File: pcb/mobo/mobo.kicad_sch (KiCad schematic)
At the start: 66 parts, among them J1 SWD_10, J2 PEEL_MOTOR, J3 DRIVE_MOTOR, J4 SW1, J5 SPRING_FINGERS, J6 SW2, J7 SW1, J8 USART1, J9 SWD_10, U1 STM32F031C6Tx, U2 STM32F031K6Ux, U4 AP1117-33, U5 MC34063AD, U6 MAX3078E, U7 DRV8837, U8 DRV8837, Y1 8MHz

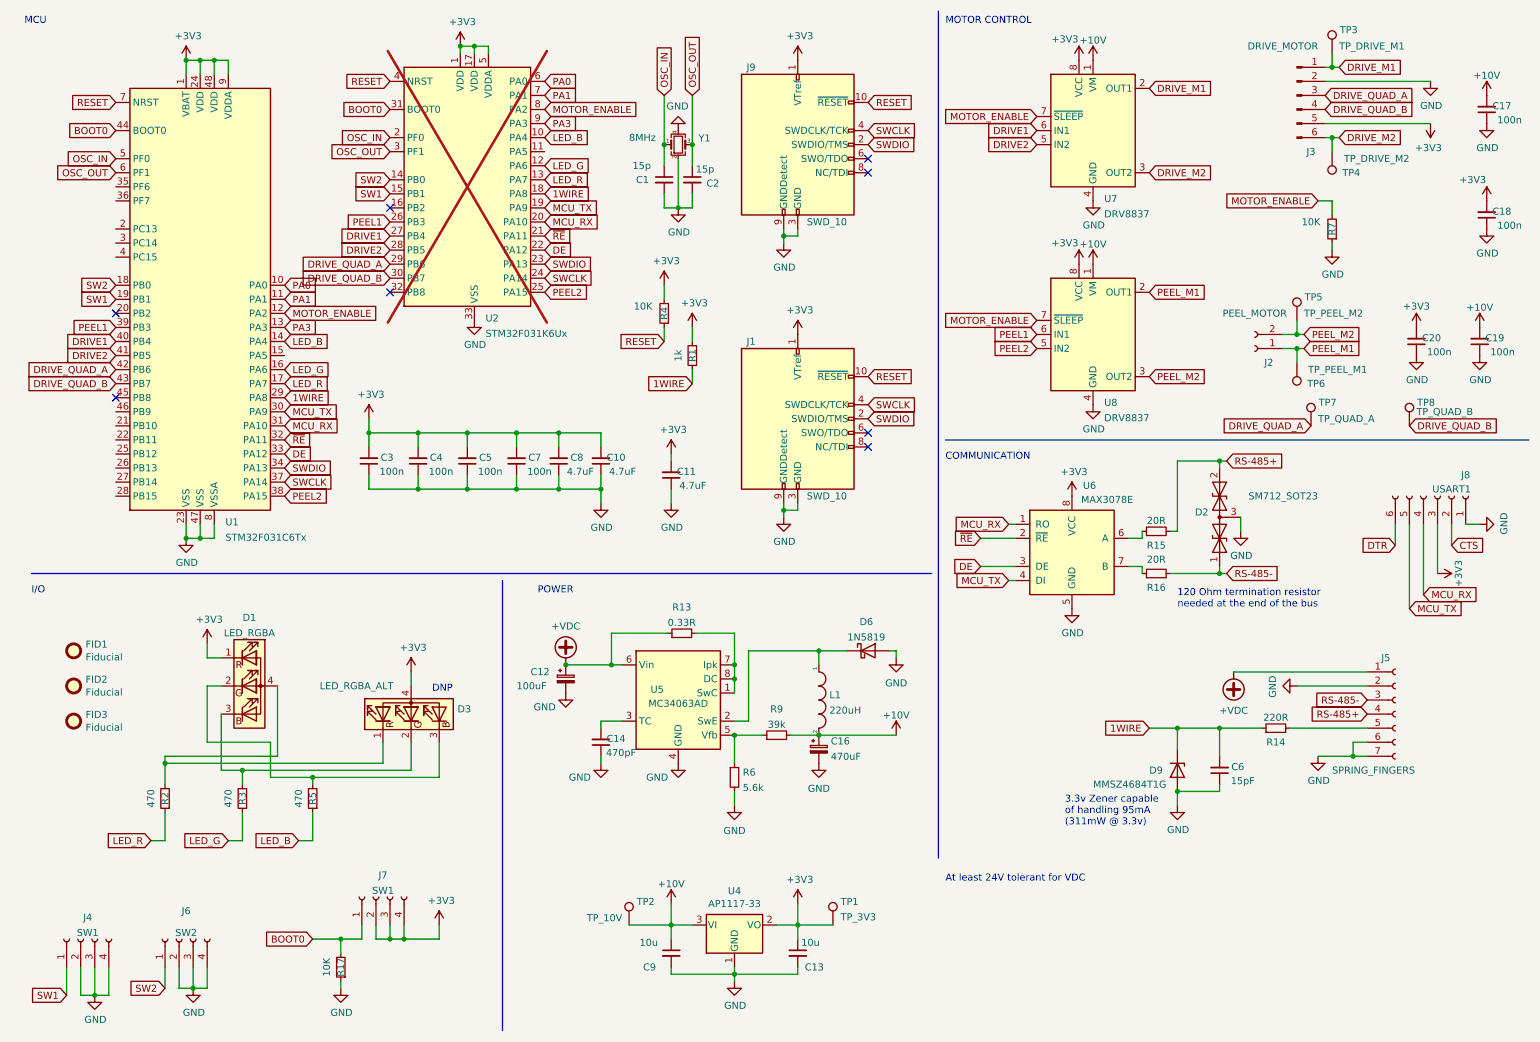
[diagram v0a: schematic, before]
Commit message: Cost optimize main feeder pcb
- Change mcu/logic supply to 5V instead of 3.3V
- Use atmega328p as mcu
- Use SP308xE as RS485 transceiver
- Use 100uF output capacitor for buck coverter
- Make it possible to use solderable standoffs instead of chamfers
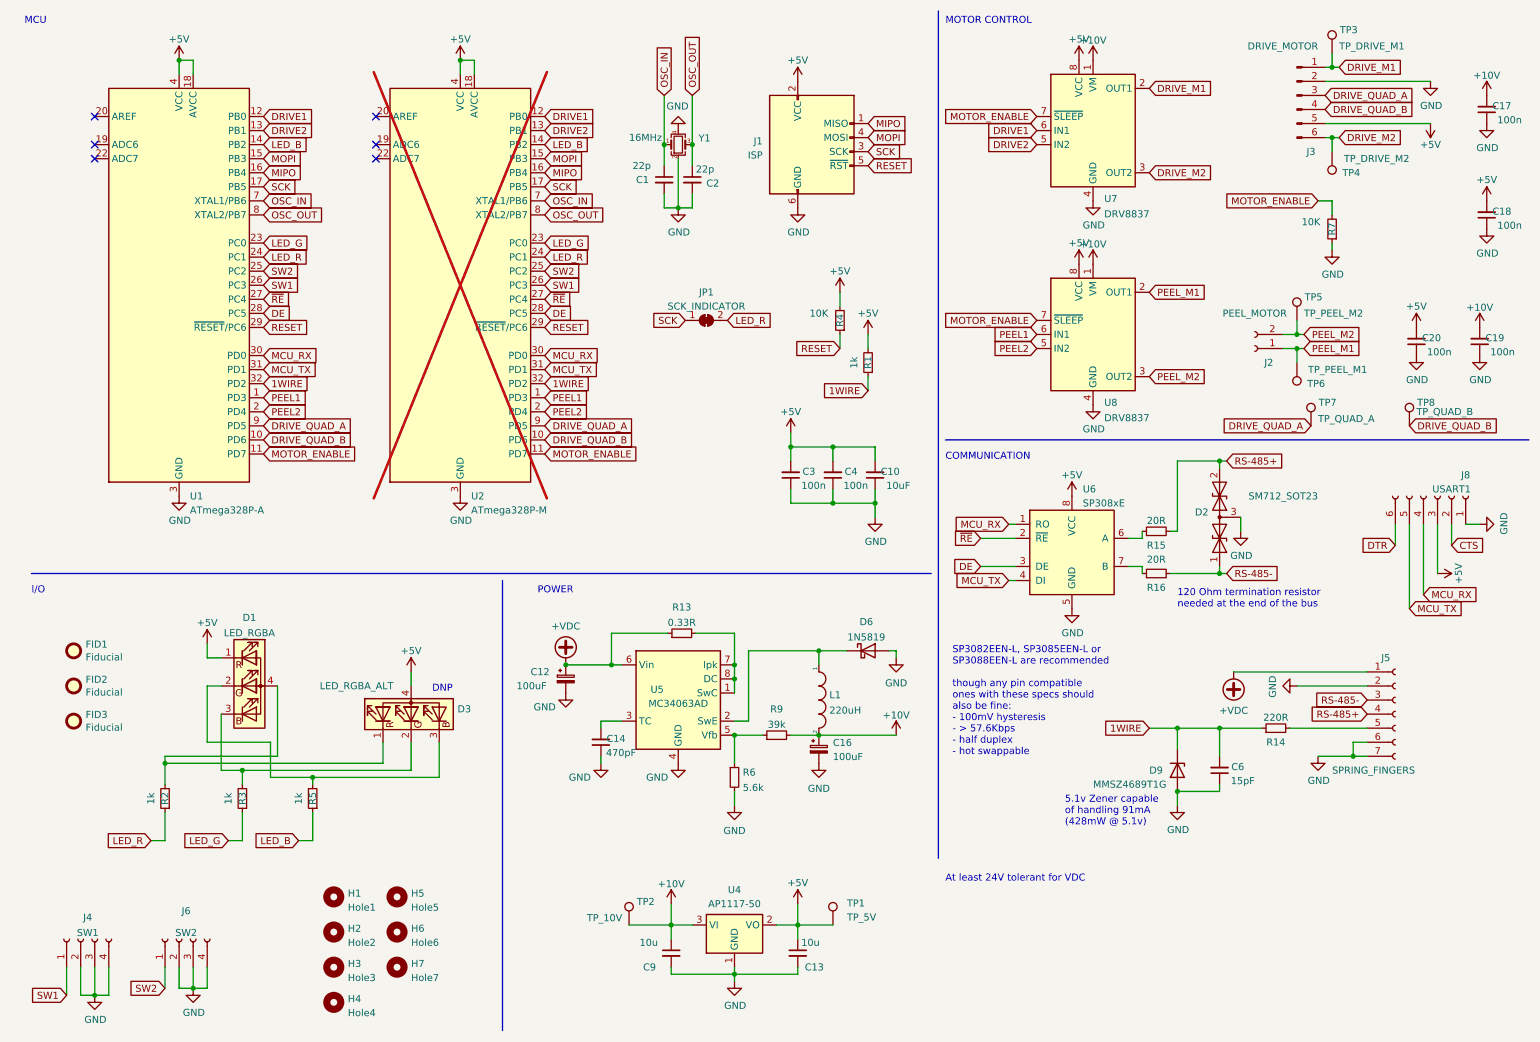
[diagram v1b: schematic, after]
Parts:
- removed C11, C8: 4.7uF, Capacitor_SMD:C_0805_2012Metric, symbol Device:C_Small
- removed C5, C7: 100n, Capacitor_SMD:C_0805_2012Metric, symbol Device:C_Small
- removed J1, J9: SWD_10, Connector_PinHeader_1.27mm:PinHeader_2x05_P1.27mm_Vertical_SMD, symbol Connector:Conn_ARM_JTAG_SWD_10
- removed J7: SW1, feeder:1TS003B-1400-3500A-CT, symbol Connector:Conn_01x04_Female
- removed R17: 10K, Resistor_SMD:R_0805_2012Metric, symbol Device:R_Small
- removed U1: STM32F031C6Tx, Package_QFP:LQFP-48_7x7mm_P0.5mm, symbol MCU_ST_STM32F0:STM32F031C6Tx
- removed U2: STM32F031K6Ux, Package_DFN_QFN:QFN-32-1EP_5x5mm_P0.5mm_EP3.45x3.45mm, symbol MCU_ST_STM32F0:STM32F031K6Ux
- removed U4: AP1117-33, Package_TO_SOT_SMD:SOT-223-3_TabPin2, symbol Regulator_Linear:AP1117-33
- removed U6: MAX3078E, Package_SO:SOIC-8_3.9x4.9mm_P1.27mm, symbol Interface_UART:MAX3078E
- added H1: Hole1, feeder:MountingHole_4.2mm_24822, symbol Mechanical:MountingHole
- added H2: Hole2, feeder:MountingHole_4.2mm_24822, symbol Mechanical:MountingHole
- added H3: Hole3, feeder:MountingHole_4.2mm_24822, symbol Mechanical:MountingHole
- added H4: Hole4, feeder:MountingHole_4.2mm_24822, symbol Mechanical:MountingHole
- added H5: Hole5, feeder:MountingHole_4.2mm_24822, symbol Mechanical:MountingHole
- added H6: Hole6, feeder:MountingHole_4.2mm_24822, symbol Mechanical:MountingHole
- added H7: Hole7, feeder:MountingHole_4.2mm_24822, symbol Mechanical:MountingHole
- added J1: ISP, feeder:ISP_FRICTION_FIT, symbol Connector:AVR-ISP-6
- added JP1: SCK_INDICATOR, Jumper:SolderJumper-2_P1.3mm_Bridged_RoundedPad1.0x1.5mm, symbol Jumper:SolderJumper_2_Bridged
- added U1: ATmega328P-A, Package_QFP:TQFP-32_7x7mm_P0.8mm, symbol MCU_Microchip_ATmega:ATmega328P-A
- added U2: ATmega328P-M, Package_DFN_QFN:QFN-32-1EP_5x5mm_P0.5mm_EP3.1x3.1mm, symbol MCU_Microchip_ATmega:ATmega328P-M
- added U4: AP1117-50, Package_TO_SOT_SMD:SOT-223-3_TabPin2, symbol Regulator_Linear:AP1117-50
- added U6: SP308xE, Package_SO:SOIC-8_3.9x4.9mm_P1.27mm, symbol feeder:SP3088E
- C1, C2: value 15p -> 22p
- C10: value 4.7uF -> 10uF
- C16: value 470uF -> 100uF
- D9: value MMSZ4684T1G -> MMSZ4689T1G
- R2, R3, R5: value 470 -> 1k
- TP1: value TP_3V3 -> TP_5V
- Y1: value 8MHz -> 16MHz
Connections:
- net +10V: now also U4.3 (VI)
- net 1WIRE: now also U1.32 (PD2), U2.32 (PD2)
- net DE: now also U1.28 (PC5), U2.28 (PC5), U6.3 (DE)
- net DRIVE1: now also U1.12 (PB0), U2.12 (PB0)
- net DRIVE2: now also U1.13 (PB1), U2.13 (PB1)
- net DRIVE_QUAD_A: now also U1.9 (PD5), U2.9 (PD5)
- net DRIVE_QUAD_B: now also U1.10 (PD6), U2.10 (PD6)
- net GND: now also J1.6 (GND), U1.21 (GND), U1.3 (GND), U1.5 (GND), U2.21 (GND), U2.3 (GND), U2.33 (GND), U2.5 (GND), U4.1 (GND), U6.5 (GND)
- net LED_B: now also U1.14 (PB2), U2.14 (PB2)
- net LED_G: now also U1.23 (PC0), U2.23 (PC0)
- net LED_R: now also JP1.2 (B), U1.24 (PC1), U2.24 (PC1)
- net MCU_RX: now also U1.30 (PD0), U2.30 (PD0), U6.1 (RO)
- net MCU_TX: now also U1.31 (PD1), U2.31 (PD1), U6.4 (DI)
- net MOTOR_ENABLE: now also U1.11 (PD7), U2.11 (PD7)
- net OSC_IN: now also U1.7 (XTAL1/PB6), U2.7 (XTAL1/PB6)
- net OSC_OUT: now also U1.8 (XTAL2/PB7), U2.8 (XTAL2/PB7)
- net PEEL1: now also U1.1 (PD3), U2.1 (PD3)
- net PEEL2: now also U1.2 (PD4), U2.2 (PD4)
- net RESET: now also J1.5 (~{RST}), U1.29 (~{RESET}/PC6), U2.29 (~{RESET}/PC6)
- net SW1: now also U1.26 (PC3), U2.26 (PC3)
- net SW2: now also U1.25 (PC2), U2.25 (PC2)
- net ~{RE}: now also U1.27 (PC4), U2.27 (PC4), U6.2 (~{RE})
- net at R15.1: now also U6.6 (A)
- net at R16.1: now also U6.7 (B)
- net +3V3 renamed +5V
- net +5V: now also J1.2 (VCC), U1.18 (AVCC), U1.4 (VCC), U1.6 (VCC), U2.18 (AVCC), U2.4 (VCC), U2.6 (VCC), U4.2 (VO), U6.8 (VCC)
- new net MIPO: J1.1 (MISO), U1.16 (PB4), U2.16 (PB4)
- new net MOPI: J1.4 (MOSI), U1.15 (PB3), U2.15 (PB3)
- new net SCK: J1.3 (SCK), JP1.1 (A), U1.17 (PB5), U2.17 (PB5)
- no-connect marks 8 -> 6
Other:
- note added: "5.1v Zener capable of handling 91mA (428mW @ 5.1v)"
- note added: "SP3082EEN-L, SP3085EEN-L or SP3088EEN-L are recommended though any pin compatible ones with these specs should also be fine: - 100mV hysteresis - > 57.6Kbps - half duplex - hot swappable"
- note removed: "3.3v Zener capable of handling 95mA (311mW @ 3.3v)"
- moved on the sheet: C10, C3, C4, R1, R4
